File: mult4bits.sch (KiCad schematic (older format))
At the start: 28 parts, among them U1 plot_v1, U10 plot_v1, U11 plot_v1, U12 plot_v1, U13 plot_v1, U14 plot_v1, U15 plot_v1, U16 plot_v1, U17 mult4bits, U18 adc_bridge_4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

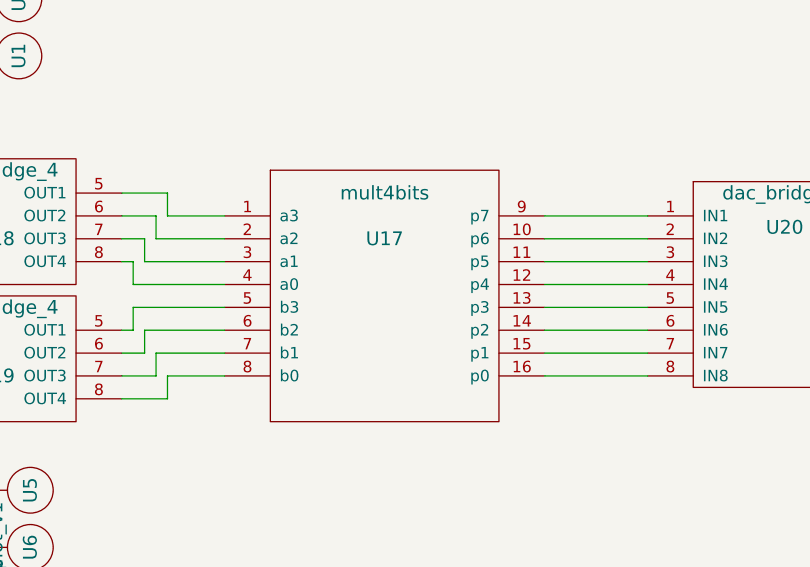
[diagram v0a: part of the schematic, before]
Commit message: 4-4 multiplier
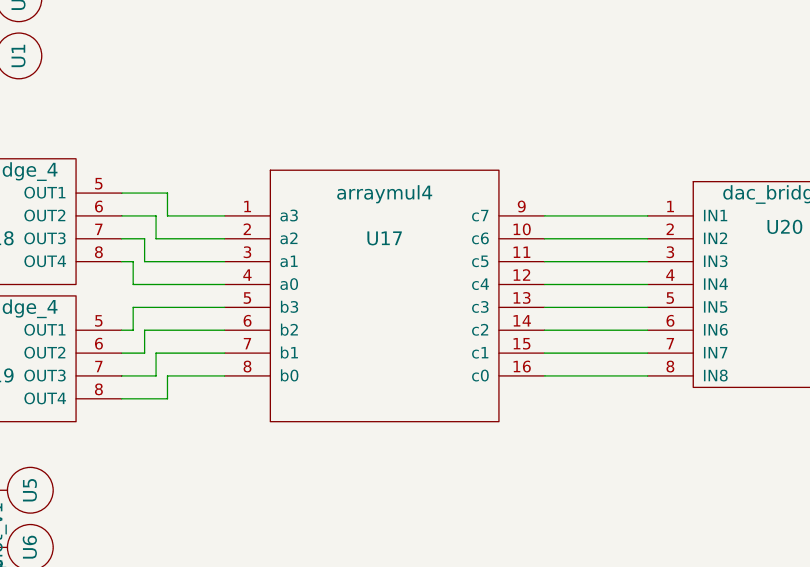
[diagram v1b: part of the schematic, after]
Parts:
- removed U17: mult4bits, symbol mult4bits
- added U17: arraymul4, symbol arraymul4
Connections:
- net at U18.5 (OUT1): now also U17.1 (a3)
- net at U20.2 (IN2): now also U17.10 (c6)
- net at U20.3 (IN3): now also U17.11 (c5)
- net at U20.4 (IN4): now also U17.12 (c4)
- net at U20.5 (IN5): now also U17.13 (c3)
- net at U20.6 (IN6): now also U17.14 (c2)
- net at U20.7 (IN7): now also U17.15 (c1)
- net at U20.8 (IN8): now also U17.16 (c0)
- net at U18.6 (OUT2): now also U17.2 (a2)
- net at U18.7 (OUT3): now also U17.3 (a1)
- net at U18.8 (OUT4): now also U17.4 (a0)
- net at U19.5 (OUT1): now also U17.5 (b3)
- net at U19.6 (OUT2): now also U17.6 (b2)
- net at U19.7 (OUT3): now also U17.7 (b1)
- net at U19.8 (OUT4): now also U17.8 (b0)
- net at U20.1 (IN1): now also U17.9 (c7)
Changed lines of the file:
@@
 $EndDescr
-$Comp
-L mult4bits U17
-U 1 1 6465AFDC
-P 2250 5450
-F 0 "U17" H 5100 7250 60  0000 C CNN
-F 1 "mult4bits" H 5100 7450 60  0000 C CNN
-F 2 "" H 5100 7400 60  0000 C CNN
-F 3 "" H 5100 7400 60  0000 C CNN
-	1    2250 5450
-	1    0    0    -1
-$EndComp
 $Comp
 L adc_bridge_4 U18
@@
 	1    0    0    -1
 $EndComp
+$Comp
+L arraymul4 U17
+U 1 1 6468FB76
+P 2250 5450
+F 0 "U17" H 5100 7250 60  0000 C CNN
+F 1 "arraymul4" H 5100 7450 60  0000 C CNN
+F 2 "" H 5100 7400 60  0000 C CNN
+F 3 "" H 5100 7400 60  0000 C CNN
+	1    2250 5450
+	1    0    0    -1
+$EndComp
